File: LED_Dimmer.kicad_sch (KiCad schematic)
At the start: 19 parts, among them J1 2.54mm Header, J2 2.54mm Header, Q1 PJA3404A_R1_00001, U1 TLC555CDR

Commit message: Fix diode part number
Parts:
- D1, D2: value 1N4148 -> 1N4148W
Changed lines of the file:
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@@
 			)
 		)
-		(property "Value" "1N4148"
+		(property "Value" "1N4148W"
 			(at 147.828 96.266 90)
 			(effects
@@
 			)
 		)
-		(property "Value" "1N4148"
+		(property "Value" "1N4148W"
 			(at 168.656 92.456 90)
 			(effects

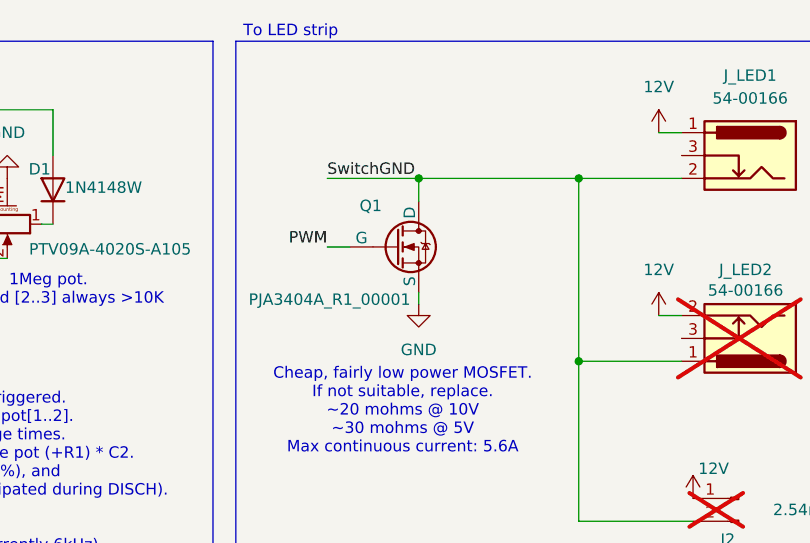
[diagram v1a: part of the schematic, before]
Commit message: Add current limiting resistor to FET
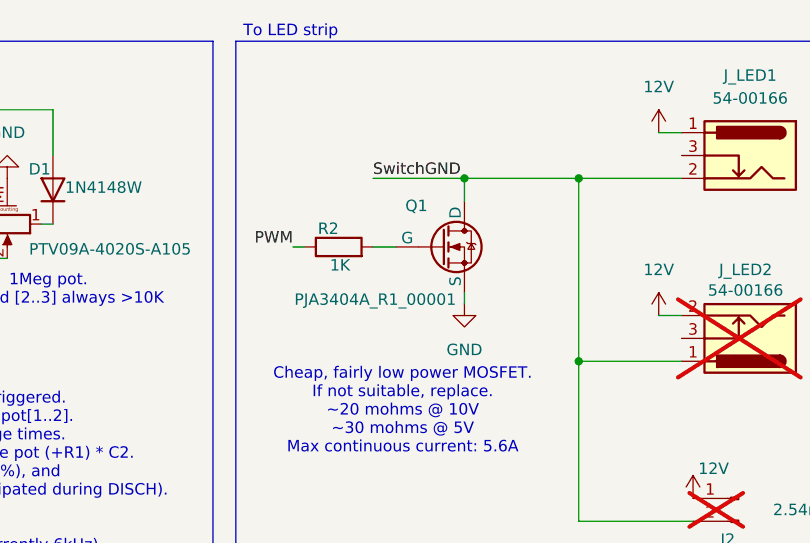
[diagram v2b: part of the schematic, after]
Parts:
- added R2: 1K, Resistor_SMD:R_0805_2012Metric_Pad1.20x1.40mm_HandSolder, symbol Device:R
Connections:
- net PWM: now also R2.1; no longer Q1.2 (G)
- new net: Q1.2 (G), R2.2
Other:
- moved on the sheet: Q1

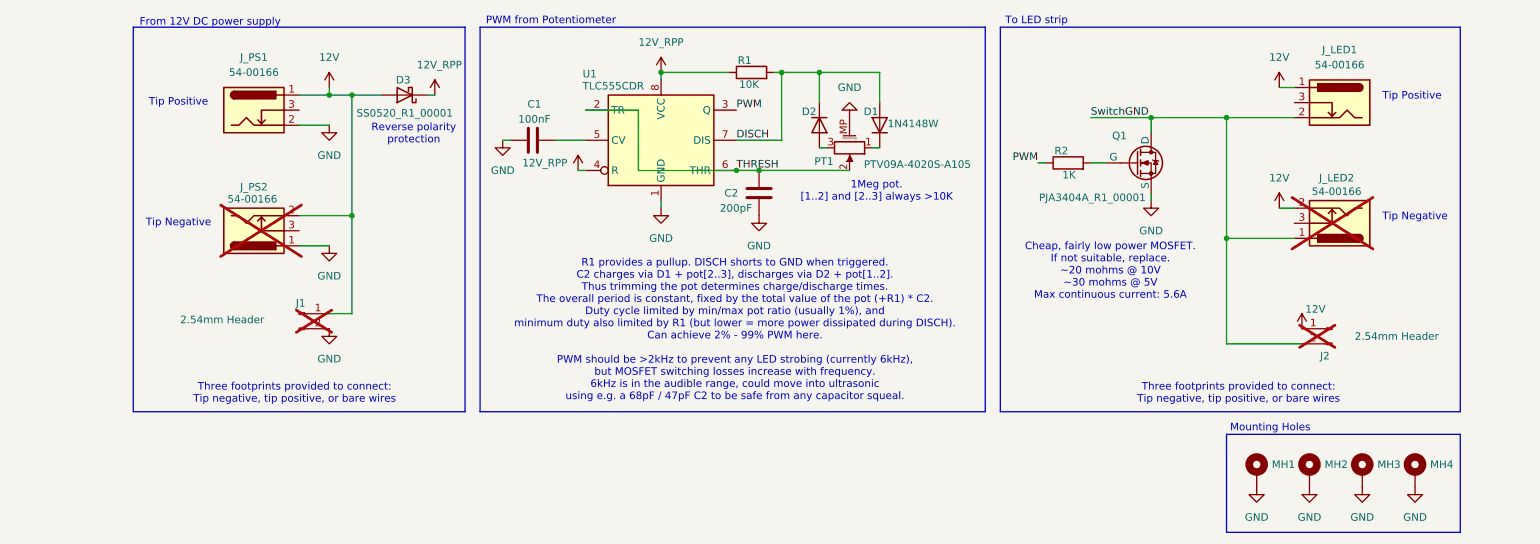
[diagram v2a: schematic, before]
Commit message: Add optional regulator for 24V LEDs
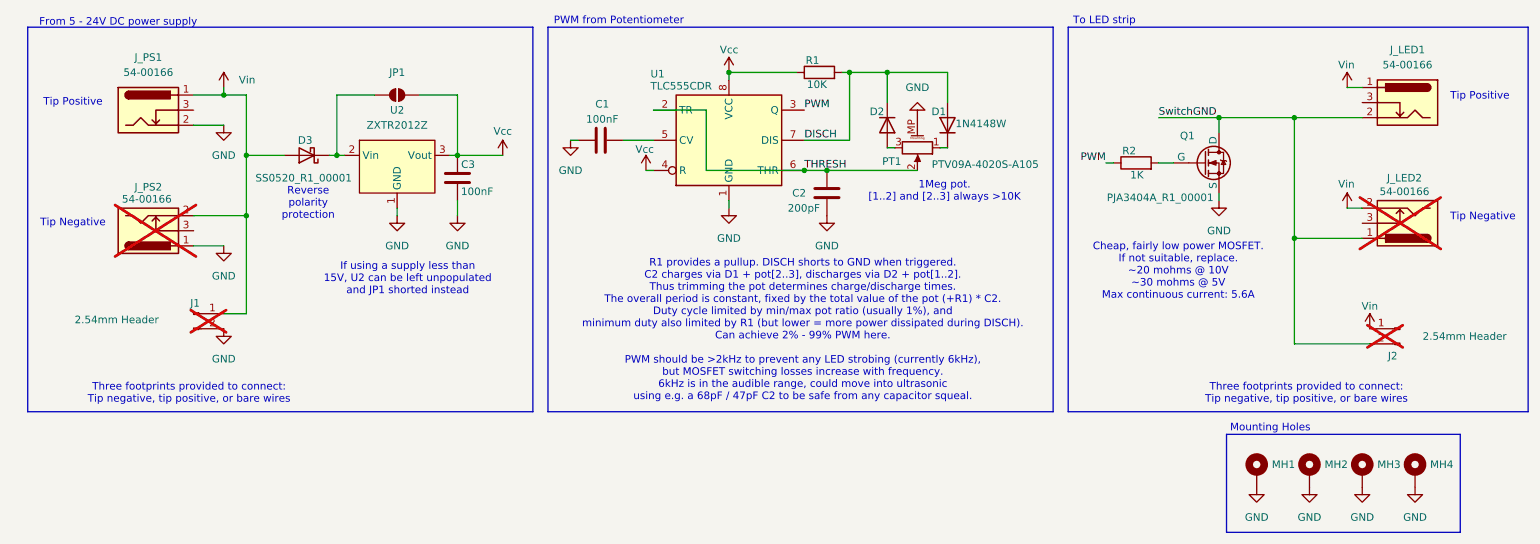
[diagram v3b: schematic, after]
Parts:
- added C3: 100nF, Capacitor_SMD:C_0805_2012Metric_Pad1.18x1.45mm_HandSolder, symbol Device:C
- added JP1: SolderJumper_2_Open, Jumper:SolderJumper-2_P1.3mm_Open_RoundedPad1.0x1.5mm, symbol Jumper:SolderJumper_2_Open
- added U2: ZXTR2012Z, Package_TO_SOT_SMD:SOT-89-3, symbol ZXTR2012Z-7:ZXTR2012Z-7
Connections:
- net GND: now also C3.1, U2.1 (GND)
- net 12V renamed Vin
- net 12V_RPP renamed Vcc
- net Vcc: now also C3.2, JP1.2 (B), U2.3 (Vout); no longer D3.1 (K)
- new net: D3.1 (K), JP1.1 (A), U2.2 (Vin)
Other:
- note added: "From 5 - 24V DC power supply"
- note added: "If using a supply less than 15V, U2 can be left unpopulated and JP1 shorted instead"
- note removed: "From 12V DC power supply"
- moved on the sheet: C1, C2, D1, D2, D3, J1, J2, J_LED1, J_LED2, J_PS1, J_PS2, PT1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

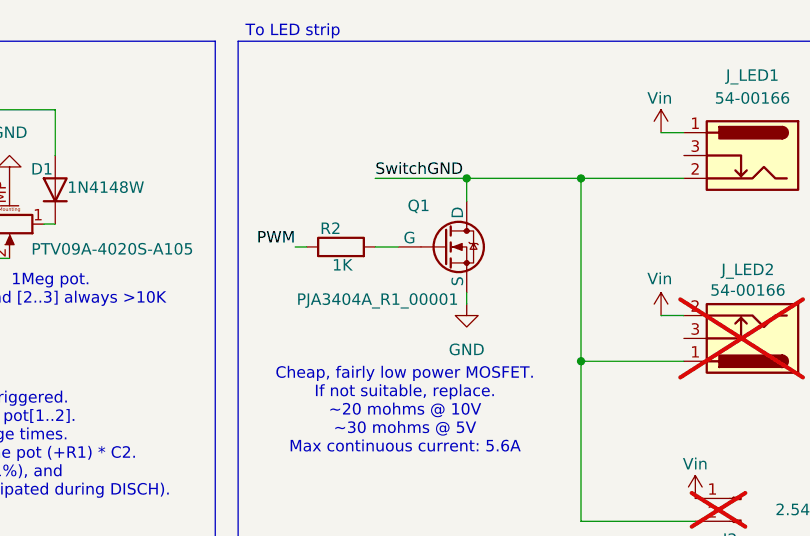
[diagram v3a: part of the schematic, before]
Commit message: Fix MOSFET pin order
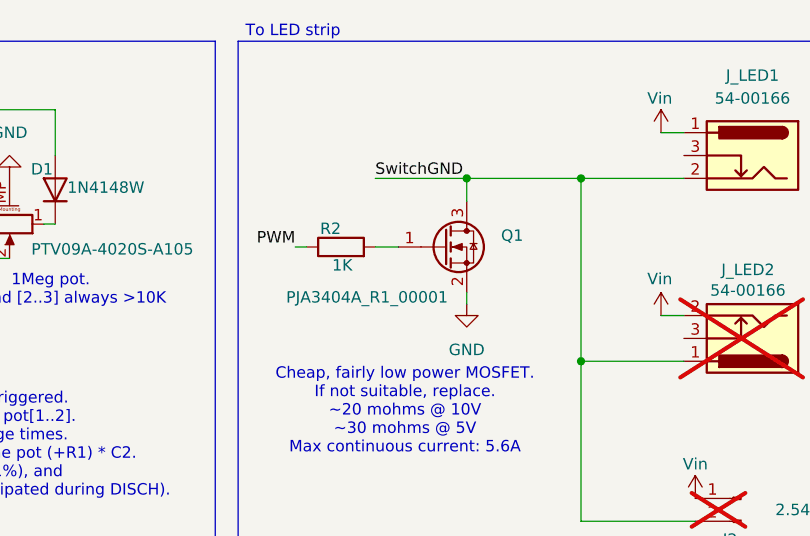
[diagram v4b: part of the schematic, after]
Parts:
- removed Q1: PJA3404A_R1_00001, Package_TO_SOT_SMD:SOT-23-3, symbol Simulation_SPICE:NMOS
- added Q1: PJA3404A_R1_00001, Package_TO_SOT_SMD:SOT-23-3, symbol Transistor_FET:Q_NMOS_GSD
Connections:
- net GND: now also Q1.2 (S)
- net SwitchGND: now also Q1.3 (D)
- net at R2.2: now also Q1.1 (G)
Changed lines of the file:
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@@
+	)
+	(symbol
+		(lib_id "Transistor_FET:Q_NMOS_GSD")
+		(at 213.36 99.06 0)
+		(unit 1)
+		(exclude_from_sim no)
+		(in_bom yes)
+		(on_board yes)
+		(dnp no)
+		(property "Reference" "Q1"
+			(at 219.71 97.7899 0)
+			(effects
+				(font
+					(size 1.27 1.27)
+				)
+				(justify left)
+			)
+		)
+		(property "Value" "PJA3404A_R1_00001"
+			(at 195.834 104.648 0)
+			(effects
+				(font
+					(size 1.27 1.27)
+				)
+				(justify left)
+			)
+		)
+		(property "Footprint" "Package_TO_SOT_SMD:SOT-23-3"
+			(at 218.44 96.52 0)
+			(effects
+				(font
+					(size 1.27 1.27)
+				)
+				(hide yes)
+			)
+		)
+		(property "Datasheet" "~"
+			(at 213.36 99.06 0)
+			(effects
+				(font
+					(size 1.27 1.27)
+				)
+				(hide yes)
+			)
+		)
+		(property "Description" "N-MOSFET transistor, gate/source/drain"
+			(at 213.36 99.06 0)
+			(effects
+				(font
+					(size 1.27 1.27)
+				)
+				(hide yes)
+			)
+		)
+		(pin "3"
+		)
+		(pin "2"
+		)
+		(pin "1"
+		)
+		(instances
+			(project ""
+				(path "/c254ffe1-0ac5-418b-b36c-0b6c5bd5ec7d"
+					(reference "Q1")
+					(unit 1)
+				)
+			)
+		)
 	)
 	(symbol
@@
 					(unit 1)
 				)
-			)
-		)
-	)
-	(symbol
-		(lib_id "Simulation_SPICE:NMOS")
-		(at 213.36 99.06 0)
-		(unit 1)
-		(exclude_from_sim no)
-		(in_bom yes)
-		(on_board yes)
-		(dnp no)
-		(property "Reference" "Q1"
-			(at 210.566 94.488 0)
-			(effects
-				(font
-					(size 1.27 1.27)
-				)
-			)
-		)
-		(property "Value" "PJA3404A_R1_00001"
-			(at 205.994 104.902 0)
-			(effects
-				(font
-					(size 1.27 1.27)
-				)
-			)
-		)
-		(property "Footprint" "Package_TO_SOT_SMD:SOT-23-3"
-			(at 218.44 96.52 0)
-			(effects
-				(font
-					(size 1.27 1.27)
-				)
-				(hide yes)
-			)
-		)
-		(property "Datasheet" "https://ngspice.sourceforge.io/docs/ngspice-html-manual/manual.xhtml#cha_MOSFETs"
-			(at 213.36 111.76 0)
-			(effects
-				(font
-					(size 1.27 1.27)
-				)
-				(hide yes)
-			)
-		)
-		(property "Description" "N-MOSFET transistor, drain/source/gate"
-			(at 213.36 99.06 0)
-			(effects
-				(font
-					(size 1.27 1.27)
-				)
-				(hide yes)
-			)
-		)
-		(property "Sim.Device" "NMOS"
-			(at 213.36 116.205 0)
-			(effects
-				(font
-					(size 1.27 1.27)
-				)
-				(hide yes)
-			)
-		)
-		(property "Sim.Type" "VDMOS"
-			(at 213.36 118.11 0)
-			(effects
-				(font
-					(size 1.27 1.27)
-				)
-				(hide yes)
-			)
-		)
-		(property "Sim.Pins" "1=D 2=G 3=S"
-			(at 213.36 114.3 0)
-			(effects
-				(font
-					(size 1.27 1.27)
-				)
-				(hide yes)
-			)
-		)
-		(pin "1"
-		)
-		(pin "3"
-		)
-		(pin "2"
-		)
-		(instances
-			(project ""
-				(path "/c254ffe1-0ac5-418b-b36c-0b6c5bd5ec7d"
-					(reference "Q1")
-					(unit 1)
-				)
